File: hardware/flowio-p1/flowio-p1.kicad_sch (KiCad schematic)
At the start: 135 parts, among them J1 DC-005, J10 VALVE, J11 VALVE, J12 VALVE, J13 VALVE, J14 VALVE, J15 VALVE, J16 VALVE, J17 VALVE, J18 DEBUG-UART, J19 DEBUG-GPIO, J2 USB-C, J5 XH-4P, J6 XH-4P, J7 XH-4P, J8 XH-4P, J9 XH-4P, Q10 AO3400A, Q11 SS8050, Q12 SS8050, Q3 AO3400A, Q4 AO3400A, Q5 AO3400A, Q6 AO3400A, Q7 AO3400A, Q8 AO3400A, Q9 AO3400A, SW1 RST, SW2 BOOT, SW3 USER, U1 ESP32-S3-WROOM-1-N16R8, U2 TCA9548APWR, U3 TPS54331DR, U4 CH340K, U5 USBLC6-2SC6

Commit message: feat(T2): 原理图 P1.1 增改 (spec v3.6 §2.1-2.4) — 11 阀板载+泵+XGZP+USB-C 供电
- J1: DC005(C431533, 缺陷#6 500mA) → TYPE-C-31-M-12(C165948) 16P 电源口:
  VBUS(A4/A9/B4/B9) 直挂 +5V (5A 路径); CC1/CC2 各 5.1k Rd 下拉 (R63/R64,
  免 PD 取 5V/3A); U7 USBLC6-2SC6 ESD 护 CC 线; D±/SBU NC; Shield→GND
- D1 (DC_IN OR 二极管) 随 DC005 移除; D2 (调试口 OR) 保留反向阻断
- J10-J17 阀驱动端子 WJ500V 螺钉 → XH2.54-2P 卧贴插座
  (footprint 字符串 JLC-MCP:CONN-TH_2P-P2.54_XH-2P, 库由 T3 建; pin1=+5V pin2=DRVx 不变)
- 新增 3 路主阀 S/V/F + 1 路泵 (1f-β): 栅阻 R55-R58 1k / 下拉 R59-R62 10k /
  Q13-Q16 AO3400 / D12-D15 SS14 飞轮 / J20-J23 XH-2P
  (编号连续化: 任务书 R59-61 空号改连续, 满足自检'新增编号连续')
- GPIO: IO15/IO16/IO17/IO18 (WROOM 引脚 8/9/10/11, 非 STRAP 未占用) → S/V/F/PUMP
- U6 XGZP6897D 板载压力传感 SOP-8: 2=+3V3 6=SDA 7=SCL 8=GND, 1/3/4/5 NC;
  C18 100nF 去耦 (与主控同 I2C 域)
- 自建内嵌符号 x3: TYPE-C-31-M-12 / WAFER-XH2_54-2PZZ / XGZP6897D (本地库缺失)
- TP13=DRV_PUMP; J18/J19 右移让位新通道列; 标题块 rev 1.1
- U5 已被 USBLC6 占用, XGZP 顺延 U6 (任务书笔误 U5); ESD=U7
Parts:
- removed D1: SS34, JLC-MCP:SMA_L4.3-W2.6-LS5.2-RD, symbol JLC-MCP:SS34_C8678
- removed J1: DC-005, JLC-MCP:DC-IN-TH_DC005, symbol JLC-MCP:DC005_C431533
- removed J10, J11, J12, J13, J14, J15, J16, J17: VALVE, JLC-MCP:CONN-TH_2P-P5.00_WJ500V-5.08-2P, symbol JLC-MCP:WJ500V-5_08-2P-14-00A
- added C18: 100nF, Capacitor_SMD:C_0603_1608Metric, symbol JLC-MCP:CL10B104KB8NNNC
- added D12, D13, D14, D15: SS14, JLC-MCP:SMA_L4.2-W2.6-LS5.0-RD_1, symbol JLC-MCP:SS14
- added J1: USB-C PWR, JLC-MCP:TYPE-C-SMD_TYPE-C-31-M-12, symbol JLC-MCP:TYPE-C-31-M-12
- added J10, J11, J12, J13, J14, J15, J16, J17, J20, J21, J22: VALVE, JLC-MCP:CONN-TH_2P-P2.54_XH-2P, symbol JLC-MCP:WAFER-XH2_54-2PZZ
- added J23: PUMP, JLC-MCP:CONN-TH_2P-P2.54_XH-2P, symbol JLC-MCP:WAFER-XH2_54-2PZZ
- added Q13, Q14, Q15, Q16: AO3400A, JLC-MCP:SOT-23-3_L2.9-W1.3-P1.90-LS2.4-BR, symbol JLC-MCP:AO3400A
- added R55, R56, R57, R58: 1k, JLC-MCP:R0603, symbol JLC-MCP:0603WAF1001T5E
- added R59, R60, R61, R62: 10k, JLC-MCP:R0603, symbol JLC-MCP:0603WAF1002T5E
- added R63, R64: 5.1k, JLC-MCP:R0603, symbol JLC-MCP:0603WAF5101T5E
- added TP13: DRV_PUMP, TestPoint:TestPoint_Pad_D1.0mm, symbol Mechanical:TestPoint
- added U6: XGZP6897D, JLC-MCP:SOP-8_L4.9-W3.9-P1.27-LS6.0-BL, symbol JLC-MCP:XGZP6897D
- added U7: USBLC6-2SC6, JLC-MCP:SOT-23-6_L2.9-W1.6-P0.95-LS2.8-BL, symbol JLC-MCP:USBLC6-2SC6
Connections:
- net +3V3: now also C18.1, U6.2 (VDD)
- net +5V: now also D12.1 (K), D13.1 (K), D14.1 (K), D15.1 (K), J1.A4 (VBUS), J1.A9 (VBUS), J1.B4 (VBUS), J1.B9 (VBUS), J10.1, J11.1, J12.1, J13.1, J14.1, J15.1, J16.1, J17.1, J20.1, J21.1, J22.1, J23.1, U7.5
- net DRV1: now also J10.2
- net DRV2: now also J11.2
- net DRV3: now also J12.2
- net DRV4: now also J13.2
- net DRV5: now also J14.2
- net DRV6: now also J15.2
- net DRV7: now also J16.2
- net DRV8: now also J17.2
- net GND: now also C18.2, J1.A1 (GND), J1.A12 (GND), J1.B1 (GND), J1.B12 (GND), J1.SH (SHIELD), Q13.2 (S), Q14.2 (S), Q15.2 (S), Q16.2 (S), R59.2, R60.2, R61.2, R62.2, R63.2, R64.2, U6.8 (GND), U7.2
- net I2C_SCL: now also U6.7 (SCL)
- net I2C_SDA: now also U6.6 (SDA)
- net IO17: now reaches U1.10 (IO17)
- net IO17: now also R57.1
- net IO18: now reaches U1.11 (IO18)
- net IO18: now also R58.1
- net IO15: now reaches U1.8 (IO15)
- net IO15: now also R55.1
- net IO16: now reaches U1.9 (IO16)
- net IO16: now also R56.1
- new net DRV_F: D14.2 (A), J22.2, Q15.3 (D)
- new net DRV_PUMP: D15.2 (A), J23.2, Q16.3 (D), TP13.1
- new net DRV_S: D12.2 (A), J20.2, Q13.3 (D)
- new net DRV_V: D13.2 (A), J21.2, Q14.3 (D)
- new net GATE_F: Q15.1 (G), R57.2, R61.1
- new net GATE_PUMP: Q16.1 (G), R58.2, R62.1
- new net GATE_S: Q13.1 (G), R55.2, R59.1
- new net GATE_V: Q14.1 (G), R56.2, R60.1
- new net P5_CC1: J1.A5 (CC1), R63.1, U7.1, U7.6
- new net P5_CC2: J1.B5 (CC2), R64.1, U7.3, U7.4
- no-connect marks 26 -> 31
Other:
- note added: "12 路 AO3400A 驱动: 8x 阀 + S/V/F 主阀 + 泵 (1f-β, XH-2P 插座 J10-J23)"
- note added: "TCA9548A 五通道 I2C 传感链 + U6 XGZP6897D 板载压力传感"
- note added: "USB-C 5A 供电 (J1: Rd 5.1k x2 + U7 ESD) + TPS54331 Buck"
- note removed: "8 路 AO3400A 阀/泵驱动 (IO4/5/6/7/10/11/12/21)"
- note removed: "FLOWIO-CN P1 电源输入 + TPS54331 Buck"
- note removed: "TCA9548A 五通道 I2C 传感链"

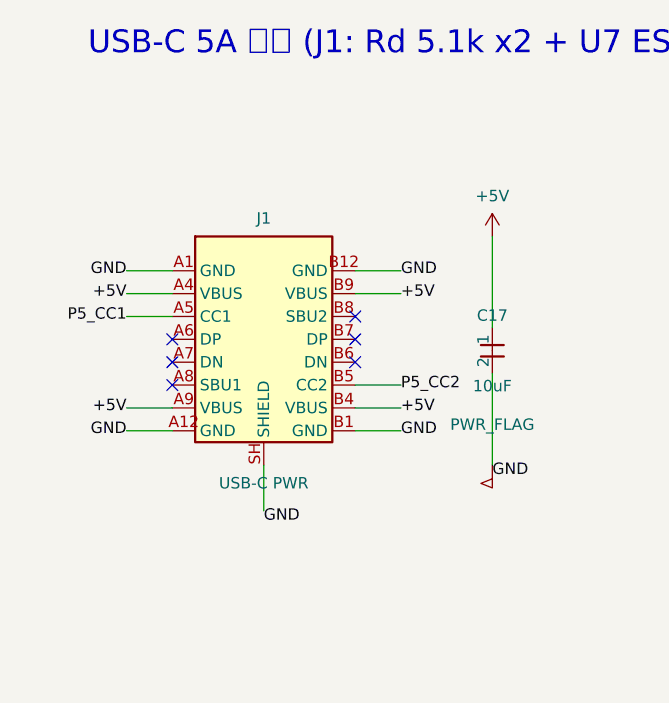
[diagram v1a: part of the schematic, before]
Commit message: feat(T3a): 封装选型回填原理图 — XH-2P=C7429671 / J1 USB-C 库符号 / U6 LOCAL 手建
- XH2.54-2P 卧贴定案 Megastar ZX-XH2.54-2PWT (C7429671, 库存 13.9 万/经济装配,
  SMD 右贴 3A, 10.0x7.8x6.2) — FP_XH2P/LCSC_XH2P 常量回填, 12x 插座 J10-J23 生效
- J1 TYPE-C-31-M-12 改用 JLC 库真符号 (装 C165948 后库内有了, 引脚名=焊盘名
  A1B12/A4B9/B1A12/B4A9/EH1-4, 自建符号防遮蔽断言使命完成退役), footprint 回填
  USB-C_SMD-TYPE-C-31-M-12_1
- U6 XGZP6897D: LCSC 无 CFSensor 现货 (JLC 扩展件 C99xxx 零库存无资料) → 淘宝件
  不入 JLC BOM; footprint=LOCAL:XGZP6897D-SOP8-W7.96-P2.54 (gen_pcb 内联生成)
- gen_pcb/make_bom ast 收集器补嵌套元组解包 + IfExp/Compare (T2 的
  for i,(x,y) 与 VALVE if PUMP else 三元表达式首次被 PCB 侧解析)
- make_bom 尾部断言随 DC005/WJ500V 移除改写 (THT 仅剩 7x XH-4P)
- ERC 0 error / 37 warning (50→37: 14 自建符号-footprint 未入库项消除);
  netlist 重导出 (net.net + fab/flowio-p1.net)
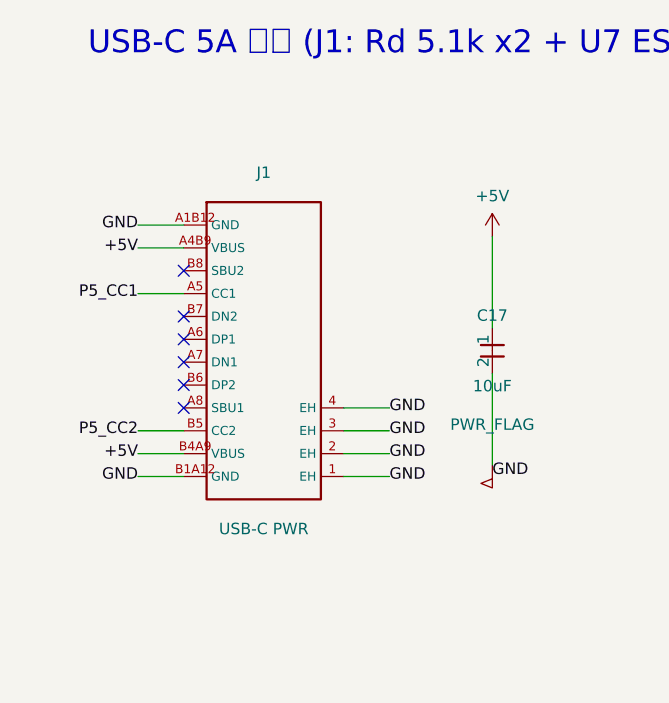
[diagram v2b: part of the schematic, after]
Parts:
- J1: footprint JLC-MCP:TYPE-C-SMD_TYPE-C-31-M-12 -> JLC-MCP:USB-C_SMD-TYPE-C-31-M-12_1
- J10, J11, J12, J13, J14, J15, J16, J17, J20, J21, J22, J23: footprint JLC-MCP:CONN-TH_2P-P2.54_XH-2P -> JLC-MCP:CONN-SMD_2P-P2.54_MEGASTAR_ZX-XH2.54-2PWT; LCSC (none) -> C7429671
- U6: footprint JLC-MCP:SOP-8_L4.9-W3.9-P1.27-LS6.0-BL -> LOCAL:XGZP6897D-SOP8-W7.96-P2.54
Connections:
- net +5V: now also J1.A4B9 (VBUS), J1.B4A9 (VBUS); no longer J1.A4 (VBUS), J1.A9 (VBUS), J1.B4 (VBUS), J1.B9 (VBUS)
- net GND: now also J1.1 (EH), J1.2 (EH), J1.3 (EH), J1.4 (EH), J1.A1B12 (GND), J1.B1A12 (GND); no longer J1.A1 (GND), J1.A12 (GND), J1.B1 (GND), J1.B12 (GND), J1.SH (SHIELD)
